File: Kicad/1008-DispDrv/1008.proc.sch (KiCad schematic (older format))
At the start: 25 parts, among them P501 CONN_9, P502 CONN_3X2, P503 CONN_4, P504 CONN_4, P505 CONN_6, P506 CONN_2, P507 CONN1X18, P508 CONN_2, U501 NX5DV330, U502 MC9S08SH32-28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

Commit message: Added silkscreen for cutouts for connectors.  Added connectors for distributing VDD.  Move connectors closer to the edge.  Add more clearance for mounting hardware.  Change connectors to right angle because of height restrictions.
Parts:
- added P509, P510, P511, P512: CONN_4, symbol CONN_4
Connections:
- wire segments 202 -> 226

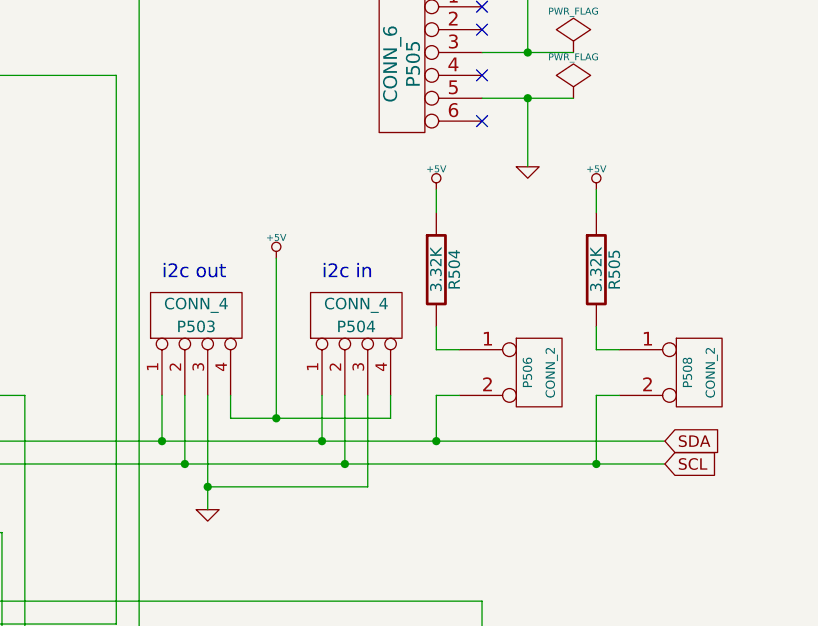
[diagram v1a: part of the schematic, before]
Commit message: Updated silkscreen.
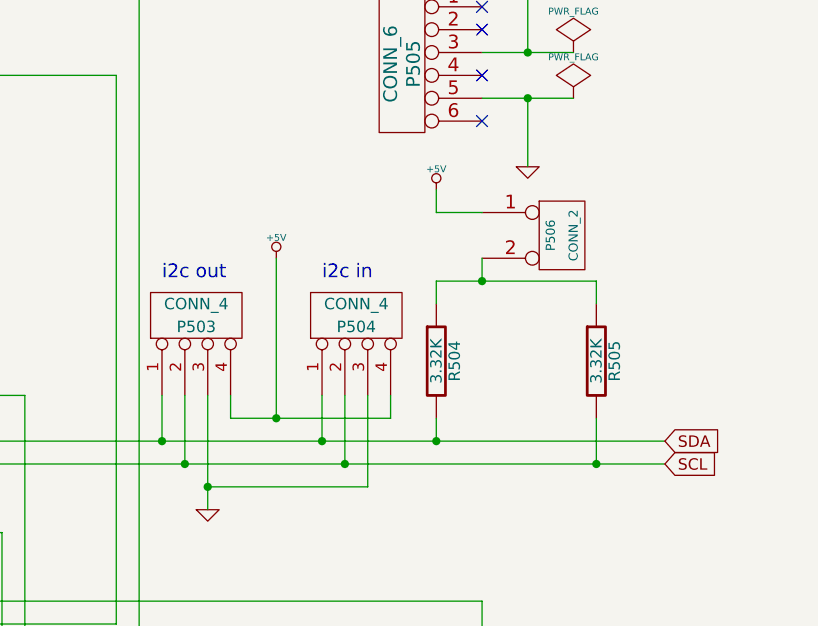
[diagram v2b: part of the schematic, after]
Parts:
- removed P508: CONN_2, symbol CONN_2
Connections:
- wire segments 226 -> 224
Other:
- moved on the sheet: P506, R504, R505

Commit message: Added code for display driver firmware (1008).  Added a boot indication LED, current limit resistor, and rs232 header support to the board.
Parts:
- added D501: LED, symbol LED
- added P508: CONN_4, symbol CONN_4
- added R506: 380, symbol R
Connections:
- wire segments 224 -> 244
- no-connect marks 11 -> 10

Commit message: Added part numbers to schematic.  Generated BOM for project.  Created spreadsheet file to total cost of project.
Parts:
- C501, C502: Distributor Mouser -> (none); Distributor PN 810-FK18X5R0J106M -> (none); Manufacturer TDK -> (none); Manufacturer PN FK18X5R0J106M -> (none); PartNum (none) -> CAP10.0u080516V
- C503, C505, C507: Distributor Mouser -> (none); Distributor PN 810-FK18X5R0J106M -> (none); Manufacturer TDK -> (none); Manufacturer PN FK18X5R0J106M -> (none); PartNum (none) -> CAP100.n0805
- C504, C506: Distributor Mouser -> (none); Distributor PN 810-FK18X5R0J106M -> (none); Manufacturer TDK -> (none); Manufacturer PN FK18X5R0J106M -> (none); PartNum (none) -> CAP1.00u080550V
- D501: PartNum (none) -> LEDRED5mmF2.0V
- P502: Distributor Mouser -> (none); Distributor PN 649-67997-472HLF -> (none); Manufacturer FCI -> (none); Manufacturer PN 67997-472HLF -> (none); PartNum (none) -> CON2x3x2.54mmVTTH
- P503, P504, P509, P510, P511, P512: PartNum (none) -> CON1x4x2.54mmRATHL
- P506: PartNum (none) -> CON1x2x2.54mmVTTH
- P508: PartNum (none) -> CON1x4x2.54mmVTTH
- R501, R502, R504, R505: Distributor Mouser -> (none); Distributor PN 279-CFR25J3K3 -> (none); Manufacturer TE Connectivity -> (none); Manufacturer PN CFR25J3K3 -> (none); PartNum (none) -> RES3.32K0805
- R503, R506: value 380 -> 383; Distributor Mouser -> (none); Distributor PN 279-CFR25J3K3 -> (none); Manufacturer TE Connectivity -> (none); Manufacturer PN CFR25J3K3 -> (none); PartNum (none) -> RES383.O0805
- RV501: PartNum (none) -> POT1.00K6mmTH
- U501, U503: PartNum (none) -> CHPNX5DV330
- U502: PartNum (none) -> PRCMC9S08SH32xWL
- VR501: PartNum (none) -> VRNADJ5.00A7.0V
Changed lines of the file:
@@
-EESchema Schematic File Version 2  date 12/3/2012 4:24:21 PM
+EESchema Schematic File Version 2  date 12/5/2012 11:19:56 AM
 LIBS:commonpart
 LIBS:power
@@
 Sheet 5 5
 Title "Display Driver"
-Date "3 dec 2012"
+Date "5 dec 2012"
 Rev "A"
 Comp "Open Pinball Project"
@@
 P 10300 3450
 F 0 "R506" V 10380 3450 50  0000 C CNN
-F 1 "380" V 10300 3450 50  0000 C CNN
-F 4 "TE Connectivity" H 10300 3450 60  0001 C CNN "Manufacturer"
-F 5 "CFR25J3K3" H 10300 3450 60  0001 C CNN "Manufacturer PN"
-F 6 "Mouser" H 10300 3450 60  0001 C CNN "Distributor"
-F 7 "279-CFR25J3K3" H 10300 3450 60  0001 C CNN "Distributor PN"
+F 1 "383" V 10300 3450 50  0000 C CNN
+F 4 "RES383.O0805" H 10300 3450 60  0001 C CNN "PartNum"
 	1    10300 3450
 	1    0    0    -1
@@
 F 0 "D501" H 10300 4100 50  0000 C CNN
 F 1 "LED" H 10300 3900 50  0000 C CNN
+F 4 "LEDRED5mmF2.0V" H 10300 4000 60  0001 C CNN "PartNum"
 	1    10300 4000
 	0    1    1    0
@@
 F 0 "P508" V 5400 6350 50  0000 C CNN
 F 1 "CONN_4" V 5500 6350 50  0000 C CNN
+F 4 "CON1x4x2.54mmVTTH" H 5450 6350 60  0001 C CNN "PartNum"
 	1    5450 6350
 	0    -1   -1   0
@@
 F 0 "P510" V 3600 7150 50  0000 C CNN
 F 1 "CONN_4" V 3700 7150 50  0000 C CNN
+F 4 "CON1x4x2.54mmRATHL" H 3650 7150 60  0001 C CNN "PartNum"
 	1    3650 7150
 	0    -1   -1   0
@@
 F 0 "P512" V 4300 7150 50  0000 C CNN
 F 1 "CONN_4" V 4400 7150 50  0000 C CNN
+F 4 "CON1x4x2.54mmRATHL" H 4350 7150 60  0001 C CNN "PartNum"
 	1    4350 7150
 	0    -1   -1   0
@@
 F 0 "P511" V 4300 6350 50  0000 C CNN
 F 1 "CONN_4" V 4400 6350 50  0000 C CNN
+F 4 "CON1x4x2.54mmRATHL" H 4350 6350 60  0001 C CNN "PartNum"
 	1    4350 6350
 	0    -1   -1   0
@@
 F 0 "P509" V 3600 6350 50  0000 C CNN
 F 1 "CONN_4" V 3700 6350 50  0000 C CNN
+F 4 "CON1x4x2.54mmRATHL" H 3650 6350 60  0001 C CNN "PartNum"
 	1    3650 6350
 	0    -1   -1   0
@@
 F 0 "R505" V 9980 2350 50  0000 C CNN
 F 1 "3.32K" V 9900 2350 50  0000 C CNN
-F 4 "TE Connectivity" H 9900 2350 60  0001 C CNN "Manufacturer"
-F 5 "CFR25J3K3" H 9900 2350 60  0001 C CNN "Manufacturer PN"
-F 6 "Mouser" H 9900 2350 60  0001 C CNN "Distributor"
-F 7 "279-CFR25J3K3" H 9900 2350 60  0001 C CNN "Distributor PN"
+F 4 "RES3.32K0805" H 9900 2350 60  0001 C CNN "PartNum"
 	1    9900 2350
 	1    0    0    -1
@@
 F 0 "R504" V 9280 2350 50  0000 C CNN
 F 1 "3.32K" V 9200 2350 50  0000 C CNN
-F 4 "TE Connectivity" H 9200 2350 60  0001 C CNN "Manufacturer"
-F 5 "CFR25J3K3" H 9200 2350 60  0001 C CNN "Manufacturer PN"
-F 6 "Mouser" H 9200 2350 60  0001 C CNN "Distributor"
-F 7 "279-CFR25J3K3" H 9200 2350 60  0001 C CNN "Distributor PN"
+F 4 "RES3.32K0805" H 9200 2350 60  0001 C CNN "PartNum"
 	1    9200 2350
 	1    0    0    -1
@@
 F 0 "P506" V 9700 1800 40  0000 C CNN
 F 1 "CONN_2" V 9800 1800 40  0000 C CNN
+F 4 "CON1x2x2.54mmVTTH" H 9750 1800 60  0001 C CNN "PartNum"
 	1    9750 1800
 	1    0    0    -1
@@
 F 0 "RV501" H 3050 7300 50  0000 C CNN
 F 1 "1.00K" H 3050 7400 50  0000 C CNN
+F 4 "POT1.00K6mmTH" H 3050 7400 60  0001 C CNN "PartNum"
 	1    3050 7400
 	0    -1   -1   0
@@
 P 2700 6850
 F 0 "R503" V 2780 6850 50  0000 C CNN
-F 1 "380" V 2700 6850 50  0000 C CNN
-F 4 "TE Connectivity" H 2700 6850 60  0001 C CNN "Manufacturer"
-F 5 "CFR25J3K3" H 2700 6850 60  0001 C CNN "Manufacturer PN"
-F 6 "Mouser" H 2700 6850 60  0001 C CNN "Distributor"
-F 7 "279-CFR25J3K3" H 2700 6850 60  0001 C CNN "Distributor PN"
+F 1 "383" V 2700 6850 50  0000 C CNN
+F 4 "RES383.O0805" H 2700 6850 60  0001 C CNN "PartNum"
 	1    2700 6850
 	1    0    0    -1
@@
 F 0 "C501" H 1150 6900 50  0000 L CNN
 F 1 "10uF" H 1150 6700 50  0000 L CNN
-F 4 "TDK" H 1100 6800 60  0001 C CNN "Manufacturer"
-F 5 "FK18X5R0J106M" H 1100 6800 60  0001 C CNN "Manufacturer PN"
-F 6 "Mouser" H 1100 6800 60  0001 C CNN "Distributor"
-F 7 "810-FK18X5R0J106M" H 1100 6800 60  0001 C CNN "Distributor PN"
+F 4 "CAP10.0u080516V" H 1100 6800 60  0001 C CNN "PartNum"
 	1    1100 6800
 	1    0    0    -1
@@
 F 0 "VR501" H 1900 7000 60  0000 C CNN
 F 1 "AME1084" H 1900 6750 60  0000 C CNN
+F 4 "VRNADJ5.00A7.0V" H 1900 6500 60  0001 C CNN "PartNum"
 	1    1900 6500
 	1    0    0    -1
@@
 F 0 "P504" V 8800 2150 50  0000 C CNN
 F 1 "CONN_4" V 8900 2150 50  0000 C CNN
+F 4 "CON1x4x2.54mmRATHL" H 8850 2150 60  0001 C CNN "PartNum"
 	1    8850 2150
 	0    -1   -1   0
@@
 F 0 "P502" H 1200 2400 50  0000 C CNN
 F 1 "CONN_3X2" V 1200 2200 40  0000 C CNN
-F 4 "FCI" H 1200 2150 60  0001 C CNN "Manufacturer"
-F 5 "67997-472HLF" H 1200 2150 60  0001 C CNN "Manufacturer PN"
-F 6 "Mouser" H 1200 2150 60  0001 C CNN "Distributor"
-F 7 "649-67997-472HLF" H 1200 2150 60  0001 C CNN "Distributor PN"
+F 4 "CON2x3x2.54mmVTTH" H 1200 2150 60  0001 C CNN "PartNum"
 	1    1200 2150
 	1    0    0    -1
@@
 F 0 "C502" H 2250 3000 50  0000 L CNN
 F 1 "10uF" H 2250 2800 50  0000 L CNN
-F 4 "TDK" H 2200 2900 60  0001 C CNN "Manufacturer"
-F 5 "FK18X5R0J106M" H 2200 2900 60  0001 C CNN "Manufacturer PN"
-F 6 "Mouser" H 2200 2900 60  0001 C CNN "Distributor"
-F 7 "810-FK18X5R0J106M" H 2200 2900 60  0001 C CNN "Distributor PN"
+F 4 "CAP10.0u080516V" H 2200 2900 60  0001 C CNN "PartNum"
 	1    2200 2900
 	1    0    0    -1
@@
 F 0 "R501" V 1880 2550 50  0000 C CNN
 F 1 "3.32K" V 1800 2550 50  0000 C CNN
-F 4 "TE Connectivity" H 1800 2550 60  0001 C CNN "Manufacturer"
-F 5 "CFR25J3K3" H 1800 2550 60  0001 C CNN "Manufacturer PN"
-F 6 "Mouser" H 1800 2550 60  0001 C CNN "Distributor"
-F 7 "279-CFR25J3K3" H 1800 2550 60  0001 C CNN "Distributor PN"
+F 4 "RES3.32K0805" H 1800 2550 60  0001 C CNN "PartNum"
 	1    1800 2550
 	1    0    0    -1
@@
 F 0 "R502" V 2130 2550 50  0000 C CNN
 F 1 "3.32K" V 2050 2550 50  0000 C CNN
-F 4 "TE Connectivity" H 2050 2550 60  0001 C CNN "Manufacturer"
-F 5 "CFR25J3K3" H 2050 2550 60  0001 C CNN "Manufacturer PN"
-F 6 "Mouser" H 2050 2550 60  0001 C CNN "Distributor"
-F 7 "279-CFR25J3K3" H 2050 2550 60  0001 C CNN "Distributor PN"
+F 4 "RES3.32K0805" H 2050 2550 60  0001 C CNN "PartNum"
 	1    2050 2550
 	1    0    0    -1
@@
 F 0 "U502" H 5400 3800 60  0000 C CNN
 F 1 "MC9S08SH32-28" H 5400 3600 60  0000 C CNN
+F 4 "PRCMC9S08SH32xWL" H 5400 2900 60  0001 C CNN "PartNum"
 	1    5400 2900
 	1    0    0    -1
@@
 F 0 "U501" H 1900 5250 60  0000 C CNN
 F 1 "NX5DV330" H 1900 5150 60  0000 C CNN
+F 4 "CHPNX5DV330" H 1900 4650 60  0001 C CNN "PartNum"
 	1    1900 4650
 	1    0    0    -1
@@
 F 0 "U503" H 8400 5250 60  0000 C CNN
 F 1 "NX5DV330" H 8400 5150 60  0000 C CNN
+F 4 "CHPNX5DV330" H 8400 4650 60  0001 C CNN "PartNum"
 	1    8400 4650
 	1    0    0    -1
@@
 F 0 "C503" H 2650 3000 50  0000 L CNN
 F 1 ".1uF" H 2650 2800 50  0000 L CNN
-F 4 "TDK" H 2600 2900 60  0001 C CNN "Manufacturer"
-F 5 "FK18X5R0J106M" H 2600 2900 60  0001 C CNN "Manufacturer PN"
-F 6 "Mouser" H 2600 2900 60  0001 C CNN "Distributor"
-F 7 "810-FK18X5R0J106M" H 2600 2900 60  0001 C CNN "Distributor PN"
+F 4 "CAP100.n0805" H 2600 2900 60  0001 C CNN "PartNum"
 	1    2600 2900
 	1    0    0    -1
@@
 F 0 "C504" H 2950 4200 50  0000 L CNN
 F 1 "1uF" H 2950 4000 50  0000 L CNN
-F 4 "TDK" H 2900 4100 60  0001 C CNN "Manufacturer"
-F 5 "FK18X5R0J106M" H 2900 4100 60  0001 C CNN "Manufacturer PN"
-F 6 "Mouser" H 2900 4100 60  0001 C CNN "Distributor"
-F 7 "810-FK18X5R0J106M" H 2900 4100 60  0001 C CNN "Distributor PN"
+F 4 "CAP1.00u080550V" H 2900 4100 60  0001 C CNN "PartNum"
 	1    2900 4100
 	1    0    0    -1
@@
 F 0 "C505" H 3250 4200 50  0000 L CNN
 F 1 ".1uF" H 3250 4000 50  0000 L CNN
-F 4 "TDK" H 3200 4100 60  0001 C CNN "Manufacturer"
-F 5 "FK18X5R0J106M" H 3200 4100 60  0001 C CNN "Manufacturer PN"
-F 6 "Mouser" H 3200 4100 60  0001 C CNN "Distributor"
-F 7 "810-FK18X5R0J106M" H 3200 4100 60  0001 C CNN "Distributor PN"
+F 4 "CAP100.n0805" H 3200 4100 60  0001 C CNN "PartNum"
 	1    3200 4100
 	1    0    0    -1
@@
 F 0 "C506" H 9550 4200 50  0000 L CNN
 F 1 "1uF" H 9550 4000 50  0000 L CNN
-F 4 "TDK" H 9500 4100 60  0001 C CNN "Manufacturer"
-F 5 "FK18X5R0J106M" H 9500 4100 60  0001 C CNN "Manufacturer PN"
-F 6 "Mouser" H 9500 4100 60  0001 C CNN "Distributor"
-F 7 "810-FK18X5R0J106M" H 9500 4100 60  0001 C CNN "Distributor PN"
+F 4 "CAP1.00u080550V" H 9500 4100 60  0001 C CNN "PartNum"
 	1    9500 4100
 	1    0    0    -1
@@
 F 0 "C507" H 9850 4200 50  0000 L CNN
 F 1 ".1uF" H 9850 4000 50  0000 L CNN
-F 4 "TDK" H 9800 4100 60  0001 C CNN "Manufacturer"
-F 5 "FK18X5R0J106M" H 9800 4100 60  0001 C CNN "Manufacturer PN"
-F 6 "Mouser" H 9800 4100 60  0001 C CNN "Distributor"
-F 7 "810-FK18X5R0J106M" H 9800 4100 60  0001 C CNN "Distributor PN"
+F 4 "CAP100.n0805" H 9800 4100 60  0001 C CNN "PartNum"
 	1    9800 4100
 	1    0    0    -1
@@
 F 0 "P503" V 8100 2150 50  0000 C CNN
 F 1 "CONN_4" V 8200 2150 50  0000 C CNN
+F 4 "CON1x4x2.54mmRATHL" H 8150 2150 60  0001 C CNN "PartNum"
 	1    8150 2150
 	0    -1   -1   0
